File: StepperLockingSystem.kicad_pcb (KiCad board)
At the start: 4 copper layers, 35.5 x 35.5 mm, 77 parts, among them J1 Conn_01x01_Female, J2 Conn_01x01_Female, J3 Conn_01x04_Male, J4 I2C_External, J6 Conn_TempMotor, SW4 SW_Reset, U1 TC1185, U2 SN65HVD232, U3 TMC2209-LA, U5 STM32F103RETx, U6 AS5600, U7 INA180A1, Y1 ABM3B-16MHz

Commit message: [WIP] Create PCB
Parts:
- removed C40, C41: 100nF 35V, Capacitor_SMD:C_0603_1608Metric
- removed J4: I2C_External, Connector_Molex:Molex_PicoBlade_53047-0410_1x04_P1.25mm_Vertical
- removed J6: Conn_TempMotor, Connector_Molex:Molex_PicoBlade_53047-0210_1x02_P1.25mm_Vertical
- removed J_CAN1, J_CAN2: Molex PicoBlade 4Pin, Connector_Molex:Molex_PicoBlade_53047-0410_1x04_P1.25mm_Vertical
- removed OPT1: SX3340, stepperservo:Omron_SX_3340
- removed R23: 10k, Resistor_SMD:R_0603_1608Metric
- removed SW4: SW_Reset, standardContent:SW_SPST_PTS636_SM25F
- added C29: 470pF 100V, Capacitor_SMD:C_0603_1608Metric, F.Cu at (164.0, 86.5)
- added C31: 470pF 100V, Capacitor_SMD:C_0603_1608Metric, F.Cu at (171.4, 79.0)
- added C32: 470pF 100V, Capacitor_SMD:C_0603_1608Metric, F.Cu at (154.4, 94.4)
- added C36: 22nF 50V, Capacitor_SMD:C_0603_1608Metric, F.Cu at (158.4, 96.3)
- added C37: 2.2uF 16V, Capacitor_SMD:C_0603_1608Metric, F.Cu at (168.0, 84.0)
- added C38: 100nF 35V, Capacitor_SMD:C_0603_1608Metric, F.Cu at (168.0, 81.5)
- added J_LED1: Molex PicoBlade, Connector_Molex:Molex_PicoBlade_53047-0410_1x04_P1.25mm_Vertical, F.Cu at (76.4, 19.6)
- added L1: XGL6060-103, Inductor_SMD:L_Coilcraft_XAL60xx_6.36x6.56mm, F.Cu at (196.0, 35.8)
- added Q1: IRF8707, Package_SO:SOIC-8_3.9x4.9mm_P1.27mm, F.Cu at (196.3, 28.5)
- added R17: 1k, Resistor_SMD:R_0603_1608Metric, F.Cu at (160.0, 84.9)
- added R18: 4.7k, Resistor_SMD:R_0603_1608Metric, F.Cu at (160.0, 87.4)
- added R8: 2k, Resistor_SMD:R_0603_1608Metric, F.Cu at (45.8, 57.9)
- added SW1: SW_Reset, extraFootprints:PTS636_F-leads, F.Cu at (42.8, 47.7)
- added U4: AS5600, Package_SO:SOIC-8_3.9x4.9mm_P1.27mm, F.Cu at (41.8, 53.4)
- C10: value 10uF 35V -> 180uF; footprint Capacitor_SMD:C_1206_3216Metric -> Capacitor_THT:CP_Radial_D8.0mm_P2.50mm; moved to F.Cu
- C11: value 10uF 35V -> 22uF; footprint Capacitor_SMD:C_1206_3216Metric -> Capacitor_SMD:C_0805_2012Metric; moved to F.Cu
- C12, C13: value 100nF 35V -> 22uF; footprint Capacitor_SMD:C_0603_1608Metric -> Capacitor_SMD:C_0805_2012Metric; moved to F.Cu
- C14: value 100nF 35V -> 1uF; moved to F.Cu
- C15: value 22nF 50V -> 1u; moved to F.Cu
- C16: value 2.2uF 16V -> 100n; moved to F.Cu
- C17: value 470pF 100V -> 15pF; moved to F.Cu
- C18: value 100nF 35V -> 15pF; moved to F.Cu
- C19: value 470pF 100V -> 100nF; moved to F.Cu
- C2, C28: value 1uF 35V -> 100nF 35V
- C20: value 470pF 100V -> 1uF; moved to F.Cu
- C21: value 100nF 35V -> 100nF; moved to F.Cu
- C22: value 470pF 100V -> 10uF; footprint Capacitor_SMD:C_0603_1608Metric -> Capacitor_SMD:C_1206_3216Metric; moved to F.Cu
- C23: value 100nF 35V -> 100nF
- C24: value 100nF 35V -> 1uF 35V
- C25, C27: value 100nF 35V -> 10uF 35V; footprint Capacitor_SMD:C_0603_1608Metric -> Capacitor_SMD:C_1206_3216Metric
- C3: value 470pF 100V -> 100nF 35V
- C30: value 10nF -> 470pF 100V
- C33: value 15pF -> 330uF 35V; footprint Capacitor_SMD:C_0603_1608Metric -> Capacitor_SMD:CP_Elec_10x10.5
- C34: value 15pF -> 100nF 35V
- C5: value 10uF 35V -> 470pF 100V; footprint Capacitor_SMD:C_1206_3216Metric -> Capacitor_SMD:C_0603_1608Metric
- C6: value 330uF 35V -> 1uF 35V; footprint Capacitor_SMD:CP_Elec_10x10.5 -> Capacitor_SMD:C_0603_1608Metric
- C7: value 100nF 35V -> 1uF
- C8: value 100nF 35V -> 22u 16V; footprint Capacitor_SMD:C_0603_1608Metric -> Capacitor_SMD:C_0805_2012Metric; moved to F.Cu
- C9: value 1uF 35V -> 22u 16V; footprint Capacitor_SMD:C_0603_1608Metric -> Capacitor_SMD:C_0805_2012Metric
- D1: footprint standardContent:LED_LiteOn_LTST-C195TGKRKT -> extraFootprints:LED_LiteOn_LTST-C195TGKRKT
- J1: value Conn_01x01_Female -> Conn_12V; footprint TestPoint:TestPoint_Loop_D2.54mm_Drill1.5mm_Beaded -> Connector_AMASS:AMASS_XT30U-M_1x02_P5.0mm_Vertical
- J2: value Conn_01x01_Female -> Conn_TempMotor; footprint TestPoint:TestPoint_Loop_D2.54mm_Drill1.5mm_Beaded -> Connector_Molex:Molex_PicoBlade_53047-0210_1x02_P1.25mm_Vertical
- R1: value 0.11 -> 10k; footprint Resistor_SMD:R_0612_1632Metric -> Resistor_SMD:R_0603_1608Metric
- R10: value 270m -> 380R; footprint Resistor_SMD:R_0612_1632Metric -> Resistor_SMD:R_0603_1608Metric; moved to F.Cu
- R11: value 10k -> 220R; moved to F.Cu
- R12: value 4k7 -> 10k
- R13: value 4k7 -> 100R
- R14: value 2k -> 100k
- R15: value 2k -> 1.1R 0.5W; footprint Resistor_SMD:R_0603_1608Metric -> Resistor_SMD:R_0805_2012Metric
- R16: value 220 -> 22k; moved to F.Cu
- R19: value 100 -> 13k
- R2: value 120 -> 51m; footprint Resistor_SMD:R_0603_1608Metric -> Resistor_SMD:R_0612_1632Metric
- R20: value 10k -> 180m; footprint Resistor_SMD:R_0603_1608Metric -> Resistor_SMD:R_0612_1632Metric; moved to F.Cu
- R21: value 380 -> 180m; footprint Resistor_SMD:R_0603_1608Metric -> Resistor_SMD:R_0612_1632Metric
- R22: value 220 -> 22k
- R3: value 1.1R 0.5W -> 2k2; footprint Resistor_SMD:R_0805_2012Metric -> Resistor_SMD:R_0603_1608Metric
- R4: value 1k -> 2k2
- R5: value 22k -> 39k; moved to F.Cu
- R6: value 4.7k -> 7k5
- R7: value 22k -> 10k; moved to F.Cu
- R9: value 270m -> 2k; footprint Resistor_SMD:R_0612_1632Metric -> Resistor_SMD:R_0603_1608Metric; moved to F.Cu
- U1: value TC1185 -> INA180A1
- U2: value SN65HVD232 -> TC1185; footprint Package_SO:SOIC-8_3.9x4.9mm_P1.27mm -> Package_TO_SOT_SMD:SOT-23-5; moved to F.Cu
- U3: value TMC2209-LA -> RT8298ZSP; footprint Package_DFN_QFN:QFN-28-1EP_5x5mm_P0.5mm_EP3.35x3.35mm_ThermalVias -> Package_SO:HSOP-8-1EP_3.9x4.9mm_P1.27mm_EP2.41x3.1mm_ThermalVias; moved to F.Cu
- U5: value STM32F103RETx -> 24LC64; footprint Package_QFP:LQFP-64_10x10mm_P0.5mm -> Package_TO_SOT_SMD:SOT-23-5; moved to F.Cu
- U6: value AS5600 -> STM32G0B1KET; footprint Package_SO:SOIC-8_3.9x4.9mm_P1.27mm -> Package_QFP:LQFP-32_7x7mm_P0.8mm; moved to F.Cu
- U7: value INA180A1 -> TMC2209-LA; footprint Package_TO_SOT_SMD:SOT-23-5 -> Package_DFN_QFN:QFN-28-1EP_5x5mm_P0.5mm_EP3.35x3.35mm_ThermalVias
- moved J_SWD1 145.8 mm to (28.7, 59.6), turned to 0 degrees
- moved U5 135.8 mm to (34.4, 64.0), turned to 0 degrees
- moved U6 132.9 mm to (31.9, 50.9), turned to 0 degrees
- moved H4 126.1 mm to (98.0, 13.3)
- moved J1 125.7 mm to (77.5, 12.9)
- moved D1 125.1 mm to (49.4, 59.9), turned to 0 degrees
- moved J2 123.2 mm to (40.0, 59.7)
- moved R14 120.2 mm to (48.0, 51.7), turned to 0 degrees
- moved C23 119.5 mm to (61.4, 46.4), turned to 0 degrees
- moved U1 118.9 mm to (84.4, 27.4), turned to 0 degrees
- moved Y1 116.2 mm to (51.7, 47.8), turned to 0 degrees
- moved C3 115.9 mm to (93.0, 25.5), turned to 0 degrees
- moved C2 115.1 mm to (89.0, 26.4), turned to 0 degrees
- moved R2 114.6 mm to (104.0, 11.8), turned to 0 degrees
- moved U2 113.4 mm to (93.2, 19.5), turned to 0 degrees
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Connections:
- C10 pad 1: VCC -> +5V
- C11 pad 1: VCC -> +5V
- C12 pad 1: VCC -> +5V
- C12 pad 2: /StepperDriver/chargePumpVoltage -> GND
- C13 pad 1: VCC -> +5V
- C14 pad 1: VCC -> Net-(C14-Pad1)
- C15 pad 1: /StepperDriver/chargePumpIn -> +3V3
- C15 pad 2: /StepperDriver/chargePumpOut -> GND
- C16 pad 1: /StepperDriver/internal5VReg -> +3V3
- C17 pad 1: /StepperDriver/coilA_2 -> GND
- C17 pad 2: GND -> Net-(C17-Pad2)
- C18 pad 1: /StepperDriver/senseCoilA -> GND
- C18 pad 2: GND -> Net-(C18-Pad2)
- C19 pad 1: /StepperDriver/coilA_1 -> /MCU/~{RST}
- C2 pad 1: +5V -> /inputCurrent
- C20 pad 1: /StepperDriver/coilB_1 -> +3V3
- C21 pad 1: /StepperDriver/senseCoilB -> +3V3
- C22 pad 1: /StepperDriver/coilB_2 -> GND
- C22 pad 2: GND -> +3V3
- C24 pad 1: GND -> VCC
- C24 pad 2: +3V3 -> Net-(C24-Pad2)
- C25 pad 1: GND -> VCC
- C25 pad 2: +3V3 -> GND
- C26 pad 1: GND -> VCC
- C26 pad 2: +3V3 -> GND
- C27 pad 1: GND -> VCC
- C27 pad 2: +3V3 -> GND
- C28 pad 1: +3V3 -> VCC
- C3 pad 1: Net-(C3-Pad1) -> /inputCurrent
- C30 pad 1: +3V3 -> /StepperDriver/coilA_1
- C33 pad 1: GND -> VCC
- C33 pad 2: Net-(C33-Pad2) -> GND
- C34 pad 1: GND -> +3V3
- C34 pad 2: Net-(C34-Pad2) -> GND
- C35 pad 1: /MCU/~{RST} -> VCC
- C35 pad 2: GND -> /StepperDriver/chargePumpVoltage
- C39 pad 1: +3V3 -> /StepperDriver/senseCoilB
- C4 pad 1: +3V3 -> +5V
- C5 pad 1: GND -> Net-(C5-Pad1)
- C5 pad 2: +3V3 -> GND
- C6 pad 1: VCC -> +3V3
- C7 pad 1: /inputCurrent -> Net-(C7-Pad1)
- C7 pad 2: GND -> Net-(C7-Pad2)
- C8 pad 1: +3V3 -> VCC
- C9 pad 2: Net-(C9-Pad2) -> GND
- J2 pad 1: GND -> +3V3
- J_SWD1 pad 5: /MCU/SWO -> unconnected-(J_SWD1-Pad5)
- R1 pad 1: VCC -> /inputCurrent
- R1 pad 2: Net-(J1-Pad1) -> Net-(R1-Pad2)
- R10 pad 1: GND -> /MCU/LED_RED
- R10 pad 2: /StepperDriver/senseCoilB -> Net-(D1-Pad2)
- R11 pad 1: /StepperDriver/Vref -> /MCU/LED_GREEN
- R11 pad 2: GND -> Net-(D1-Pad1)
- R12 pad 1: /MCU/I2C2_SCL -> /MCU/tempMotor
- R12 pad 2: +3V3 -> GND
- R13 pad 1: +3V3 -> Net-(R13-Pad1)
- R13 pad 2: /MCU/I2C2_SDA -> Net-(C17-Pad2)
- R14 pad 1: +3V3 -> /MCU/SWCLK
- R14 pad 2: /MCU/I2C1_SDA -> GND
- R15 pad 1: +3V3 -> Net-(C24-Pad2)
- R15 pad 2: /MCU/I2C1_SCL -> GND
- R16 pad 1: +5V -> +3V3
- R16 pad 2: Net-(OPT1-Pad1) -> /MCU/~{Stepper_Enable}
- R19 pad 1: Net-(R19-Pad1) -> +3V3
- R19 pad 2: Net-(C33-Pad2) -> /StepperDriver/Vref
- R2 pad 1: Net-(J_CAN1-Pad2) -> VCC
- R2 pad 2: Net-(J_CAN1-Pad1) -> Net-(J1-Pad1)
- R20 pad 1: /MCU/tempMotor -> GND
- R20 pad 2: GND -> /StepperDriver/senseCoilA
- R21 pad 1: /MCU/LED_RED -> GND
- R21 pad 2: Net-(D1-Pad2) -> /StepperDriver/senseCoilB
- R22 pad 1: /MCU/LED_GREEN -> /StepperDriver/Vref
- R22 pad 2: Net-(D1-Pad1) -> GND
- R3 pad 1: Net-(C9-Pad2) -> +5V
- R3 pad 2: GND -> /ledData
- R4 pad 1: Net-(R4-Pad1) -> +5V
- R4 pad 2: /MCU/Stepper_UART -> /ledClock
- R5 pad 1: +3V3 -> +5V
- R5 pad 2: /StepperDriver/~{EN} -> VCC
- R6 pad 1: Net-(R4-Pad1) -> VCC
- R6 pad 2: +3V3 -> GND
- R7 pad 1: +3V3 -> /enableBuck
- R7 pad 2: /StepperDriver/Vref -> GND
- R9 pad 1: GND -> +3V3
- R9 pad 2: /StepperDriver/senseCoilA -> /MCU/I2C1_SDA
- U1 pad 1: +5V -> Net-(R1-Pad2)
- U1 pad 3: +5V -> Net-(J1-Pad1)
- U1 pad 4: Net-(C3-Pad1) -> VCC
- U2 pad 1: /CAN_TX -> +5V
- U2 pad 3: +3V3 -> +5V
- U2 pad 4: /CAN_RX -> Net-(C5-Pad1)
- U2 pad 5: (no net) -> +3V3
- U3 pad 1: /StepperDriver/coilB_2 -> Net-(C7-Pad2)
- U3 pad 2: /StepperDriver/~{EN} -> Net-(C7-Pad1)
- U3 pad 3: GND -> Net-(C14-Pad1)
- U3 pad 4: /StepperDriver/chargePumpOut -> Net-(Q1-Pad4)
- U3 pad 5: /StepperDriver/chargePumpIn -> GND
- U3 pad 6: /StepperDriver/chargePumpVoltage -> VCC
- U3 pad 7: GND -> /enableBuck
- U3 pad 8: /StepperDriver/internal5VReg -> VCC
- U5 pad 1: +3V3 -> /MCU/I2C1_SCL
- U5 pad 2: /MCU/endstopRight -> GND
- U5 pad 3: /StepperDriver/Diag -> /MCU/I2C1_SDA
- U5 pad 4: /StepperDriver/~{EN} -> +3V3
- U5 pad 5: Net-(R19-Pad1) -> GND
- U6 pad 1: +3V3 -> /MCU/LED_GREEN
- U6 pad 2: +3V3 -> Net-(R13-Pad1)
- U6 pad 3: (no net) -> Net-(C18-Pad2)
- U6 pad 4: GND -> +3V3
- U6 pad 6: /MCU/I2C1_SDA -> /MCU/~{RST}
- U6 pad 7: /MCU/I2C1_SCL -> /inputCurrent
- U6 pad 8: GND -> /MCU/tempMotor
- U7 pad 1: Net-(R23-Pad2) -> /StepperDriver/coilB_2
- U7 pad 2: GND -> /MCU/~{Stepper_Enable}
- U7 pad 3: Net-(J1-Pad1) -> GND
- U7 pad 4: VCC -> /StepperDriver/chargePumpOut
- U7 pad 5: +3V3 -> /StepperDriver/chargePumpIn
- Y1 pad 1: Net-(C34-Pad2) -> Net-(C18-Pad2)
- Y1 pad 3: Net-(C33-Pad2) -> Net-(C17-Pad2)
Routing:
- net GND: track 143.2 -> 0.00 mm, vias 40 -> 0
- net +3V3: track 138.7 -> 0.00 mm, vias 12 -> 0
- net +5V: track 85.7 -> 0.00 mm, vias 2 -> 0
- net /MCU/tempMotor: track 53.2 -> 0.00 mm, vias 5 -> 0
- net /MCU/~{RST}: track 47.2 -> 0.00 mm, vias 4 -> 0
- net /MCU/I2C2_SDA: track 33.2 -> 0.00 mm, vias 1 -> 0
- net Net-(R23-Pad2): track 29.2 -> 0.00 mm, vias 2 -> 0
- net /MCU/I2C2_SCL: track 26.7 -> 0.00 mm, vias 1 -> 0
- net /StepperDriver/~{EN}: track 26.5 -> 0.00 mm, vias 3 -> 0
- net /inputCurrent: track 23.8 -> 0.00 mm, vias 3 -> 0
- net /StepperDriver/Direction: track 22.0 -> 0.00 mm
- net /StepperDriver/Diag: track 15.1 -> 0.00 mm
- net Net-(J_CAN1-Pad2): track 14.8 -> 0.00 mm, vias 1 -> 0
- net /StepperDriver/Step: track 14.7 -> 0.00 mm
- net Net-(J_CAN1-Pad1): track 14.0 -> 0.00 mm, vias 1 -> 0
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- removed copper zone on B.Cu, net +3V3
- removed copper zone on B.Cu, net /StepperDriver/coilA_1
- removed copper zone on In1.Cu, net /StepperDriver/coilA_1
- removed copper zone on B.Cu, net /StepperDriver/coilA_2
- removed copper zone on In1.Cu, net /StepperDriver/coilA_2
- removed copper zone on B.Cu, net /StepperDriver/coilB_1
- removed copper zone on In1.Cu, net /StepperDriver/coilB_1
- removed copper zone on B.Cu, net /StepperDriver/coilB_2
- removed copper zone on In1.Cu, net /StepperDriver/coilB_2
- removed copper zone on B.Cu, net /StepperDriver/senseCoilA
- removed copper zone on B.Cu, net /StepperDriver/senseCoilB
- removed copper zone on B.Cu, net GND
- removed copper zone on F.Cu, net GND
- removed copper zone on In1.Cu, net GND
- removed copper zone on In2.Cu, net GND
- removed copper zone on F.Cu, net Net-(J1-Pad1)
- removed copper zone on B.Cu, net VCC
- removed copper zone on F.Cu, net VCC
- removed copper zone on In1.Cu, net VCC
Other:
- board outline removed
- board text removed: "2021"
- board text removed: "A1"
- board text removed: "A2"
- board text removed: "Albrecht"
- board text removed: "B1"
- board text removed: "B2"
- board text removed: "CAN"
- board text removed: "ExtSen"
- board text removed: "Gnd"
- board text removed: "SWD"
- board text removed: "Stepper Servo v1"
- board text removed: "Tmp"
- board text removed: "Vcc"

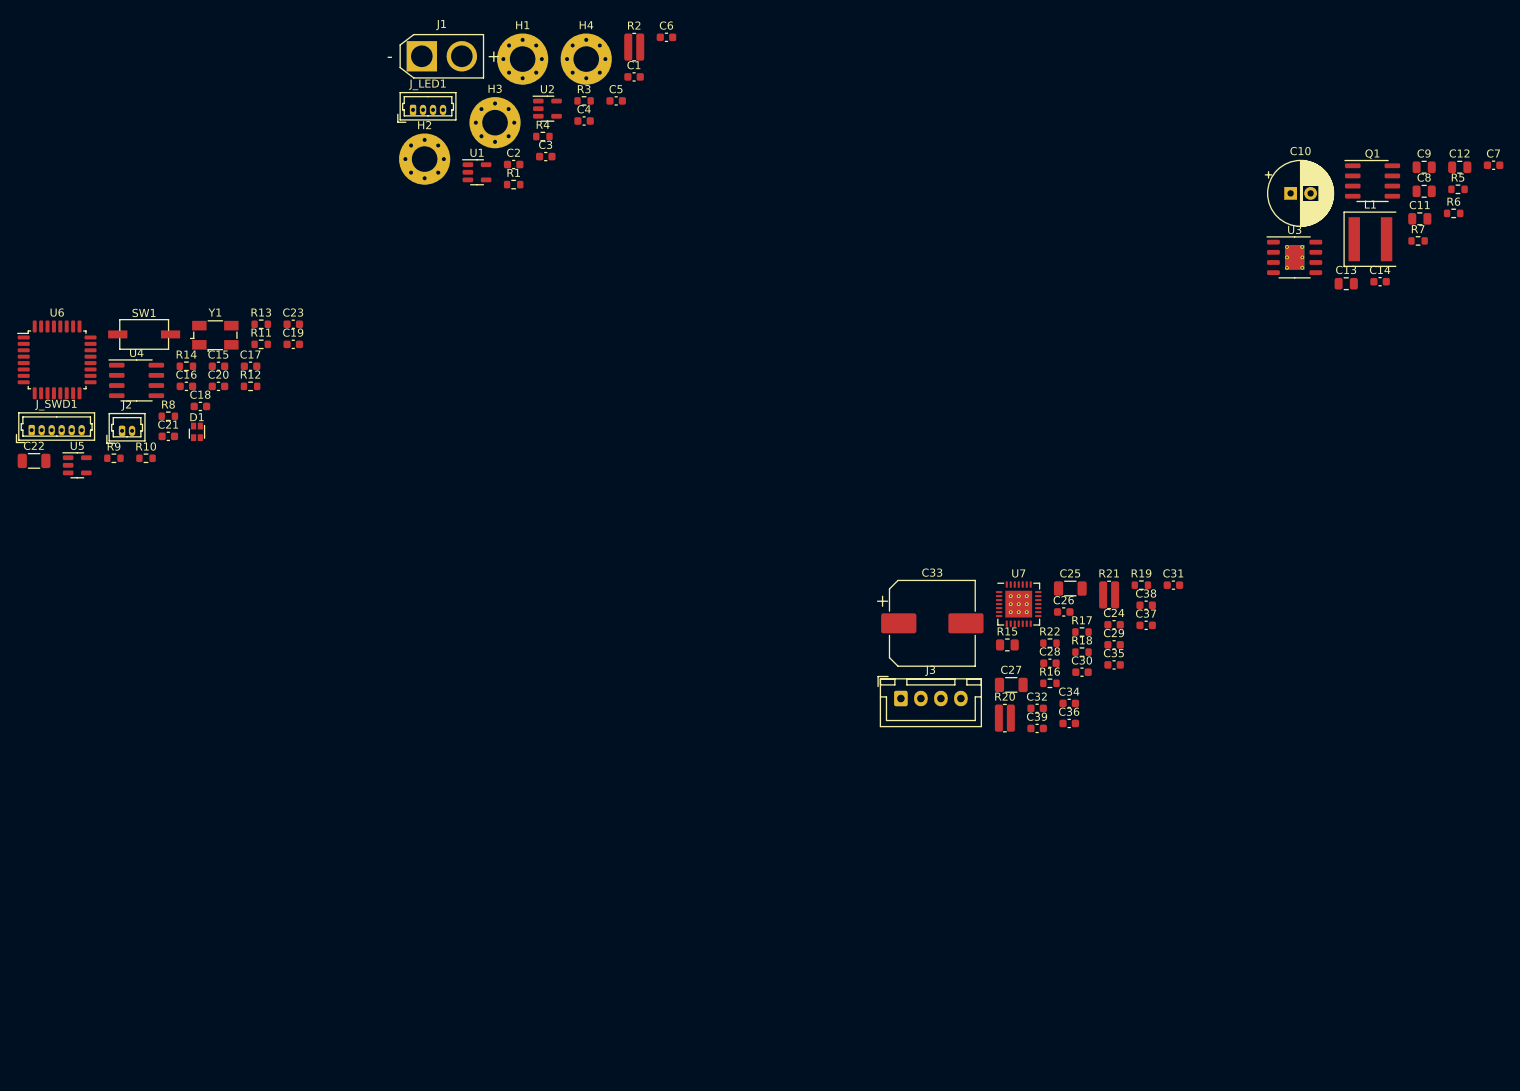
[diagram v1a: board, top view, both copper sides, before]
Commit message: Finish schematic
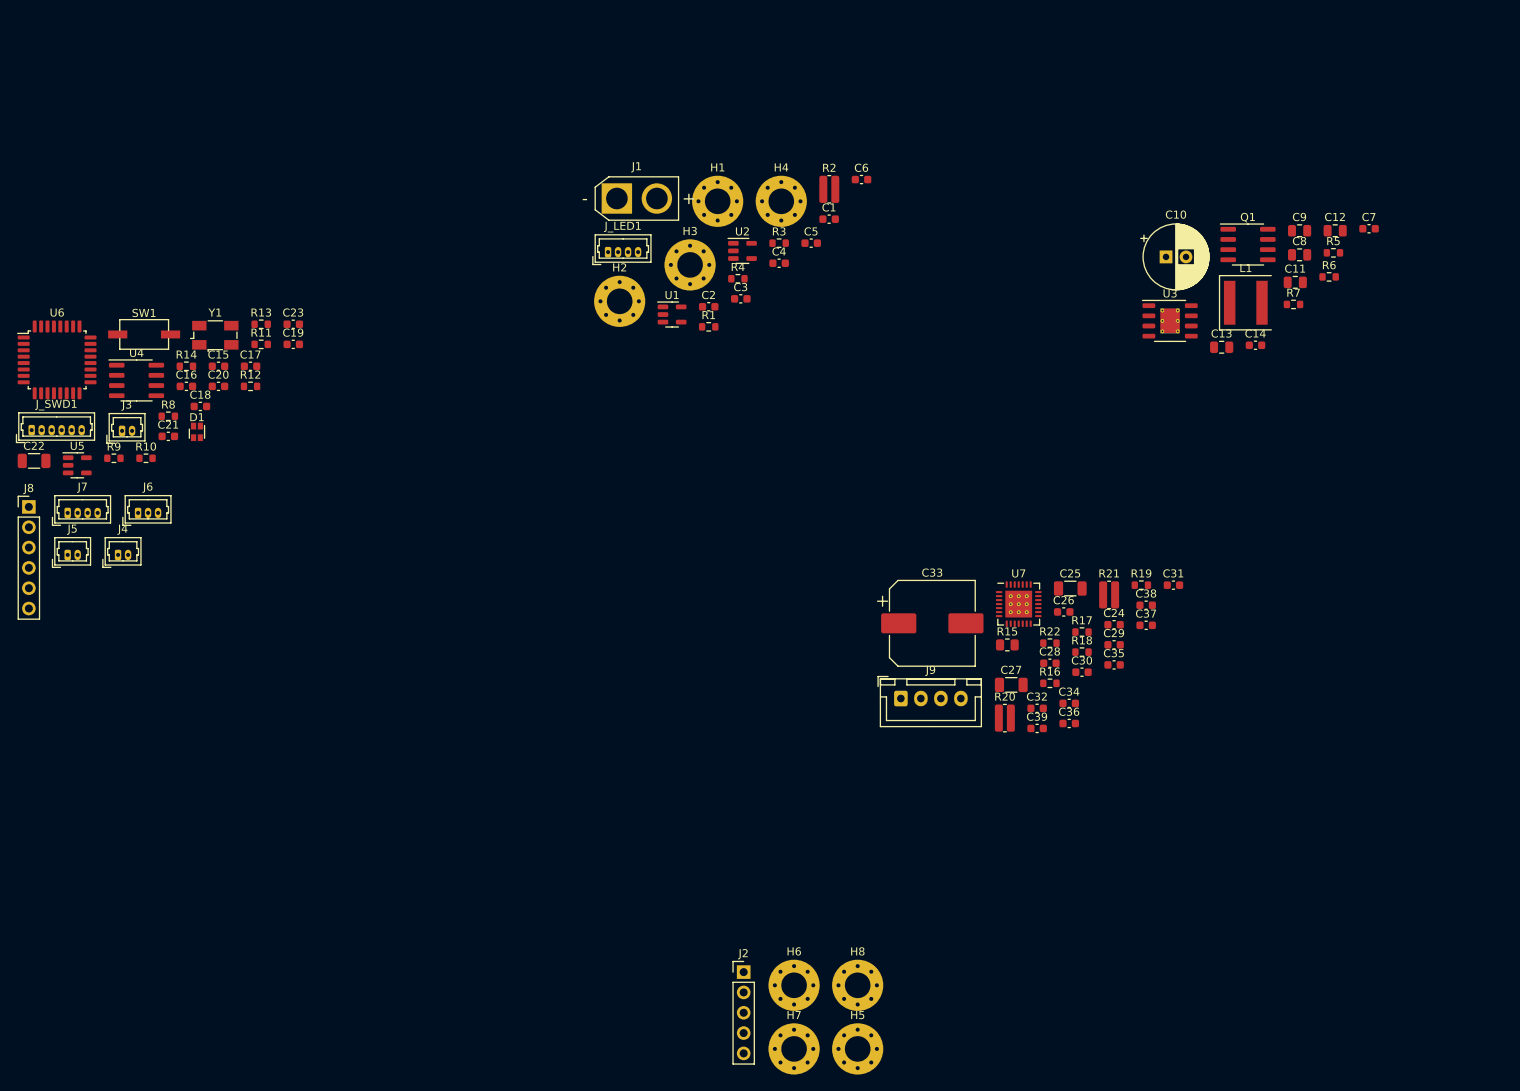
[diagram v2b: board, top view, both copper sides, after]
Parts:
- added H5: MountingHole_Pad, MountingHole:MountingHole_3.2mm_M3_Pad_Via, F.Cu at (131.9, 137.0)
- added H6: MountingHole_Pad, MountingHole:MountingHole_3.2mm_M3_Pad_Via, F.Cu at (124.0, 129.1)
- added H7: MountingHole_Pad, MountingHole:MountingHole_3.2mm_M3_Pad_Via, F.Cu at (124.0, 137.0)
- added H8: MountingHole_Pad, MountingHole:MountingHole_3.2mm_M3_Pad_Via, F.Cu at (131.9, 129.1)
- added J2: 5Pin DuPont 2.54mm, Connector_PinHeader_2.54mm:PinHeader_1x05_P2.54mm_Vertical, F.Cu at (117.7, 127.4)
- added J4: Molex PicoBlade 2Pin, Connector_Molex:Molex_PicoBlade_53047-0210_1x02_P1.25mm_Vertical, F.Cu at (39.5, 75.2)
- added J5: Molex PicoBlade 2Pin, Connector_Molex:Molex_PicoBlade_53047-0210_1x02_P1.25mm_Vertical, F.Cu at (33.2, 75.2)
- added J6: Molex PicoBlade 3Pin, Connector_Molex:Molex_PicoBlade_53047-0310_1x03_P1.25mm_Vertical, F.Cu at (42.0, 70.0)
- added J7: Molex PicoBlade 4Pin, Connector_Molex:Molex_PicoBlade_53047-0410_1x04_P1.25mm_Vertical, F.Cu at (33.2, 70.0)
- added J8: 6Pin DuPont 2.56mm, Connector_PinHeader_2.54mm:PinHeader_1x06_P2.54mm_Vertical, F.Cu at (28.4, 69.2)
- J3: renamed from J2; value Conn_TempMotor -> Molex PicoBlade 2Pin
- moved C3 30.2 mm to (117.3, 43.2)
- moved H1 30.2 mm to (114.5, 31.1)
- moved H4 30.2 mm to (122.4, 31.1)
- moved R2 30.2 mm to (128.4, 29.6)
- moved C6 30.2 mm to (132.4, 28.3)
- moved H2 30.2 mm to (102.2, 43.5)
- moved R4 30.2 mm to (117.0, 40.7)
- moved C1 30.2 mm to (128.4, 33.3)
- moved C2 30.2 mm to (113.3, 44.2)
- moved C4 30.2 mm to (122.1, 38.8)
- moved C5 30.2 mm to (126.1, 36.3)
- moved H3 30.2 mm to (111.0, 39.0)
- moved J1 30.2 mm to (101.8, 30.7)
- moved J_LED1 30.2 mm to (100.8, 37.4)
- moved R1 30.2 mm to (113.3, 46.7)
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- renumbered J3 to J9
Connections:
- U6 pad 10: /MCU/PINA3 -> /MCU/LockState
- U6 pad 12: /MCU/I³C_busy -> /MCU/PINA5
- U6 pad 15: /MCU/PINB0 -> /MCU/CloseButton
- U6 pad 16: /MCU/PINB1 -> /MCU/OpenButton
- U6 pad 17: /MCU/PINB2 -> /MCU/I³C_busy
- U6 pad 9: /MCU/PINA2 -> /MCU/DoorState

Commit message: Add many changes to schematic and WIP PCB
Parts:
- removed C35, C38, C39: 100nF 35V, Capacitor_SMD:C_0603_1608Metric
- removed C36: 22nF 50V, Capacitor_SMD:C_0603_1608Metric
- removed C37: 2.2uF 16V, Capacitor_SMD:C_0603_1608Metric
- removed H8: MountingHole_Pad, MountingHole:MountingHole_3.2mm_M3_Pad_Via
- removed L1: XGL6060-103, Inductor_SMD:L_Coilcraft_XAL60xx_6.36x6.56mm
- added D2: ESD9X5.0ST5G, Diode_SMD:D_SOD-923, F.Cu at (239.8, 99.8)
- added D3: D_Schottky, Diode_SMD:D_SOD-523, F.Cu at (106.3, 54.2)
- added D4: LTST-C195TGKRKT, extraFootprints:LED_LiteOn_LTST-C195TGKRKT, F.Cu at (171.1, 84.2)
- added F1: 2A, extraFootprints:KEYSTONE-FUSE-3557-2, F.Cu at (227.8, 102.9)
- added F2: 2A, extraFootprints:KEYSTONE-FUSE-3557-2, F.Cu at (227.8, 111.0)
- added J10: Conn_01x04_Male, Connector_JST:JST_XH_B4B-XH-A_1x04_P2.50mm_Vertical, F.Cu at (129.7, 125.2)
- added R23: 180m, Resistor_SMD:R_0612_1632Metric, B.Cu at (132.9, 118.7)
- added R24: 22k, Resistor_SMD:R_0603_1608Metric, B.Cu at (139.4, 126.7)
- added TP1: TestPoint, TestPoint:TestPoint_Pad_D2.0mm, F.Cu at (211.1, 138.6)
- added TP10: TestPoint, TestPoint:TestPoint_Pad_D2.0mm, F.Cu at (207.0, 138.6)
- added TP11: TestPoint, TestPoint:TestPoint_Pad_D2.0mm, F.Cu at (223.2, 130.5)
- added TP12: TestPoint, TestPoint:TestPoint_Pad_D2.0mm, F.Cu at (211.1, 130.5)
- added TP13: TestPoint, TestPoint:TestPoint_Pad_D2.0mm, F.Cu at (223.2, 134.6)
- added TP14: TestPoint, TestPoint:TestPoint_Pad_D2.0mm, F.Cu at (219.2, 134.6)
- added TP2: TestPoint, TestPoint:TestPoint_Pad_D2.0mm, F.Cu at (207.0, 130.5)
- added TP3: TestPoint, TestPoint:TestPoint_Pad_D2.0mm, F.Cu at (215.1, 130.5)
- added TP4: TestPoint, TestPoint:TestPoint_Pad_D2.0mm, F.Cu at (211.1, 134.6)
- added TP5: TestPoint, TestPoint:TestPoint_Pad_D2.0mm, F.Cu at (207.0, 134.6)
- added TP6: TestPoint, TestPoint:TestPoint_Pad_D2.0mm, F.Cu at (215.1, 138.6)
- added TP7: TestPoint, TestPoint:TestPoint_Pad_D2.0mm, F.Cu at (219.2, 130.5)
- added TP8: TestPoint, TestPoint:TestPoint_Pad_D2.0mm, F.Cu at (215.1, 134.6)
- added TP9: TestPoint, TestPoint:TestPoint_Pad_D2.0mm, F.Cu at (219.2, 138.6)
- C10: value 180uF -> 15pF; footprint Capacitor_THT:CP_Radial_D8.0mm_P2.50mm -> Capacitor_SMD:C_0603_1608Metric
- C11: value 22uF -> 15pF; footprint Capacitor_SMD:C_0805_2012Metric -> Capacitor_SMD:C_0603_1608Metric
- C12: value 22uF -> 100nF; footprint Capacitor_SMD:C_0805_2012Metric -> Capacitor_SMD:C_0603_1608Metric
- C13: value 22uF -> 1uF; footprint Capacitor_SMD:C_0805_2012Metric -> Capacitor_SMD:C_0603_1608Metric; moved to B.Cu
- C14: value 1uF -> 100nF; moved to B.Cu
- C15: value 1u -> 100nF
- C16: value 100n -> 100nF
- C17: value 15pF -> 10uF; footprint Capacitor_SMD:C_0603_1608Metric -> Capacitor_SMD:C_1206_3216Metric; moved to B.Cu
- C18: value 15pF -> 100nF; moved to B.Cu
- C19: value 100nF -> 1uF 16V; moved to B.Cu
- C20: value 1uF -> 10uF 16V; footprint Capacitor_SMD:C_0603_1608Metric -> Capacitor_SMD:C_1206_3216Metric; moved to B.Cu
- C21, C23: value 100nF -> 100nF 16V; moved to B.Cu
- C22: value 10uF -> 10uF 16V; moved to B.Cu
- C24: value 1uF 35V -> 470pF 100V; moved to B.Cu
- C25, C27: value 10uF 35V -> 470pF 100V; footprint Capacitor_SMD:C_1206_3216Metric -> Capacitor_SMD:C_0603_1608Metric; moved to B.Cu
- C26: value 100nF 35V -> 470pF 100V; moved to B.Cu
- C28: value 100nF 35V -> 330uF 16V; footprint Capacitor_SMD:C_0603_1608Metric -> Capacitor_SMD:CP_Elec_10x10.5
- C29, C30: value 470pF 100V -> 100nF 16V; moved to B.Cu
- C31: value 470pF 100V -> 22nF 50V; moved to B.Cu
- C32: value 470pF 100V -> 2.2uF 16V; moved to B.Cu
- C33: value 330uF 35V -> 100nF 35V; footprint Capacitor_SMD:CP_Elec_10x10.5 -> Capacitor_SMD:C_0603_1608Metric; moved to B.Cu
- C34, U7: moved to B.Cu
- C7: value 1uF -> 100n; moved to B.Cu
- C8: value 22u 16V -> 1uF 16V; footprint Capacitor_SMD:C_0805_2012Metric -> Capacitor_SMD:C_0603_1608Metric
- C9: value 22u 16V -> 1uF; footprint Capacitor_SMD:C_0805_2012Metric -> Capacitor_SMD:C_0603_1608Metric
- D1: value LTST-C195TGKRKT -> ESD9X12ST5G; footprint extraFootprints:LED_LiteOn_LTST-C195TGKRKT -> Diode_SMD:D_SOD-923
- H1, H2, H3, H4, H5, H6, H7: footprint MountingHole:MountingHole_3.2mm_M3_Pad_Via -> MountingHole:MountingHole_3.2mm_M3_ISO14580
- J1: value Conn_12V -> Phoenix Contact MSTB 4 Pin; footprint Connector_AMASS:AMASS_XT30U-M_1x02_P5.0mm_Vertical -> Connector_Phoenix_MSTB:PhoenixContact_MSTBVA_2,5_4-G-5,08_1x04_P5.08mm_Vertical
- J4: value Molex PicoBlade 2Pin -> Molex PicoBlade 4Pin; footprint Connector_Molex:Molex_PicoBlade_53047-0210_1x02_P1.25mm_Vertical -> Connector_Molex:Molex_PicoBlade_53047-0410_1x04_P1.25mm_Vertical
- J6: value Molex PicoBlade 3Pin -> 6Pin DuPont 2.56mm; footprint Connector_Molex:Molex_PicoBlade_53047-0310_1x03_P1.25mm_Vertical -> Connector_PinHeader_2.54mm:PinHeader_1x07_P2.54mm_Vertical
- J7: value Molex PicoBlade 4Pin -> Molex PicoBlade 2Pin; footprint Connector_Molex:Molex_PicoBlade_53047-0410_1x04_P1.25mm_Vertical -> Connector_Molex:Molex_PicoBlade_53047-0210_1x02_P1.25mm_Vertical
- J8: value 6Pin DuPont 2.56mm -> Molex PicoBlade 3Pin; footprint Connector_PinHeader_2.54mm:PinHeader_1x06_P2.54mm_Vertical -> Connector_Molex:Molex_PicoBlade_53047-0310_1x03_P1.25mm_Vertical
- J9: value Conn_01x04_Male -> Molex PicoBlade 2Pin; footprint Connector_JST:JST_XH_B4B-XH-A_1x04_P2.50mm_Vertical -> Connector_Molex:Molex_PicoBlade_53047-0210_1x02_P1.25mm_Vertical
- Q1: value IRF8707 -> IRLML0030; footprint Package_SO:SOIC-8_3.9x4.9mm_P1.27mm -> Package_TO_SOT_SMD:SOT-23
- R10: value 380R -> 220R
- R11: value 220R -> 10k; moved to B.Cu
- R12: value 10k -> 100k
- R13: value 100R -> 5k
- R14: value 100k -> 5k
- R15: value 1.1R 0.5W -> 5k; footprint Resistor_SMD:R_0805_2012Metric -> Resistor_SMD:R_0603_1608Metric
- R16: value 22k -> 5k
- R17: value 1k -> 1.1R 0.5W; footprint Resistor_SMD:R_0603_1608Metric -> Resistor_SMD:R_0805_2012Metric; moved to B.Cu
- R18: value 4.7k -> 22k; moved to B.Cu
- R19: value 13k -> 1k; moved to B.Cu
- R2: value 51m -> 100m 0.5W
- R20: value 180m -> 4.7k; footprint Resistor_SMD:R_0612_1632Metric -> Resistor_SMD:R_0603_1608Metric; moved to B.Cu
- R21: value 180m -> 13k; footprint Resistor_SMD:R_0612_1632Metric -> Resistor_SMD:R_0603_1608Metric; moved to B.Cu
- R22: value 22k -> 180m; footprint Resistor_SMD:R_0603_1608Metric -> Resistor_SMD:R_0612_1632Metric; moved to B.Cu
- R5: value 39k -> 2k; moved to B.Cu
- R6: value 7k5 -> 2k; moved to B.Cu
- R7: value 10k -> 1k
- R8: value 2k -> 100R
- R9: value 2k -> 380R
- U3: value RT8298ZSP -> 24LC64; footprint Package_SO:HSOP-8-1EP_3.9x4.9mm_P1.27mm_EP2.41x3.1mm_ThermalVias -> Package_TO_SOT_SMD:SOT-23-5; moved to B.Cu
- U4: value AS5600 -> STM32G0B1KET; footprint Package_SO:SOIC-8_3.9x4.9mm_P1.27mm -> Package_QFP:LQFP-32_7x7mm_P0.8mm
- U5: value 24LC64 -> USBLC6-2SC6; footprint Package_TO_SOT_SMD:SOT-23-5 -> Package_TO_SOT_SMD:SOT-23-6
- U6: value STM32G0B1KET -> USBLC6-2SC6; footprint Package_QFP:LQFP-32_7x7mm_P0.8mm -> Package_TO_SOT_SMD:SOT-23-6
- moved H7 232.5 mm to (355.2, 112.5)
- moved J2 205.6 mm to (323.2, 129.6), turned to 180 degrees
- moved C18 201.3 mm to (248.5, 89.0), turned to 180 degrees
- moved R11 201.0 mm to (255.8, 81.2), turned to 180 degrees
- moved U6 200.6 mm to (219.9, 120.9)
- moved H6 199.9 mm to (323.2, 112.5)
- moved U5 198.9 mm to (225.0, 120.9)
- moved C17 196.5 mm to (248.5, 91.2), turned to 180 degrees
- moved R14 195.5 mm to (227.2, 129.7)
- moved D1 194.9 mm to (239.8, 101.8)
- moved C15 192.8 mm to (227.2, 132.2)
- moved H5 191.3 mm to (323.2, 136.5)
- moved R13 187.7 mm to (219.0, 141.9)
- moved C16 181.6 mm to (207.0, 141.9)
- moved J_SWD1 155.4 mm to (180.6, 92.5), turned to 180 degrees
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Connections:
- C10 pad 1: +5V -> GND
- C10 pad 2: GND -> Net-(C10-Pad2)
- C11 pad 1: +5V -> GND
- C11 pad 2: GND -> Net-(C11-Pad2)
- C12 pad 1: +5V -> /MCU/~{RST}
- C13 pad 1: +5V -> +3V3
- C14 pad 1: Net-(C14-Pad1) -> +3V3
- C15 pad 1: +3V3 -> GND
- C15 pad 2: GND -> +5V
- C16 pad 1: +3V3 -> GND
- C16 pad 2: GND -> +5V
- C17 pad 2: Net-(C17-Pad2) -> +3V3
- C18 pad 2: Net-(C18-Pad2) -> +3V3
- C19 pad 1: /MCU/~{RST} -> VCC
- C19 pad 2: GND -> Net-(C19-Pad2)
- C20 pad 1: +3V3 -> VCC
- C21 pad 1: +3V3 -> VCC
- C22 pad 1: GND -> VCC
- C22 pad 2: +3V3 -> GND
- C23 pad 1: GND -> VCC
- C23 pad 2: +3V3 -> GND
- C24 pad 1: VCC -> /StepperDriver/coilA_2
- C24 pad 2: Net-(C24-Pad2) -> GND
- C25 pad 1: VCC -> /StepperDriver/coilA_1
- C26 pad 1: VCC -> /StepperDriver/coilB_1
- C27 pad 1: VCC -> /StepperDriver/coilB_2
- C29 pad 1: /StepperDriver/coilA_2 -> +3V3
- C30 pad 1: /StepperDriver/coilA_1 -> VCC
- C30 pad 2: GND -> /StepperDriver/chargePumpVoltage
- C31 pad 1: /StepperDriver/coilB_1 -> /StepperDriver/chargePumpIn
- C31 pad 2: GND -> /StepperDriver/chargePumpOut
- C32 pad 1: /StepperDriver/coilB_2 -> /StepperDriver/internal5VReg
- C33 pad 1: VCC -> /StepperDriver/senseCoilA
- C34 pad 1: +3V3 -> /StepperDriver/senseCoilB
- C7 pad 1: Net-(C7-Pad1) -> +3V3
- C7 pad 2: Net-(C7-Pad2) -> GND
- C9 pad 1: VCC -> Net-(C9-Pad1)
- D1 pad 2: Net-(D1-Pad2) -> GND
- J1 pad 1: Net-(J1-Pad1) -> Net-(F1-Pad1)
- J3 pad 1: +3V3 -> VCC
- J3 pad 2: /MCU/tempMotor -> Net-(D3-Pad2)
- J4 pad 1: /MCU/DoorState -> +3V3
- J4 pad 2: GND -> /MCU/I²C1_SCL
- J5 pad 1: /MCU/LockState -> +3V3
- J5 pad 2: GND -> /MCU/tempMotor
- J6 pad 1: /MCU/CloseButton -> +3V3
- J6 pad 2: /MCU/OpenButton -> +5V
- J6 pad 3: GND -> /MCU/PINB7
- J7 pad 1: /MCU/I²C2_SDA -> +5V
- J7 pad 2: /MCU/I²C2_SCL -> Net-(J7-Pad2)
- J8 pad 1: +3V3 -> +5V
- J8 pad 2: +5V -> Net-(J8-Pad2)
- J8 pad 3: /MCU/PINA4 -> Net-(J8-Pad3)
- J9 pad 1: /StepperDriver/coilA_2 -> +5V
- J9 pad 2: /StepperDriver/coilA_1 -> Net-(J9-Pad2)
- Q1 pad 2: GND -> Net-(C9-Pad1)
- Q1 pad 3: GND -> Net-(D3-Pad2)
- R10 pad 1: /MCU/LED_RED -> /MCU/LED_GREEN
- R10 pad 2: Net-(D1-Pad2) -> Net-(D4-Pad1)
- R11 pad 1: /MCU/LED_GREEN -> /MCU/tempMotor
- R11 pad 2: Net-(D1-Pad1) -> GND
- R12 pad 1: /MCU/tempMotor -> /MCU/SWCLK
- R13 pad 1: Net-(R13-Pad1) -> Net-(J8-Pad2)
- R13 pad 2: Net-(C17-Pad2) -> GND
- R14 pad 1: /MCU/SWCLK -> Net-(J8-Pad3)
- R15 pad 1: Net-(C24-Pad2) -> Net-(J9-Pad2)
- R16 pad 1: +3V3 -> Net-(J7-Pad2)
- R16 pad 2: /MCU/~{Stepper_Enable} -> GND
- R17 pad 1: Net-(R17-Pad1) -> Net-(C19-Pad2)
- R17 pad 2: /MCU/Stepper_UART -> GND
- R18 pad 1: Net-(R17-Pad1) -> +3V3
- R18 pad 2: +3V3 -> /MCU/~{Stepper_Enable}
- R19 pad 1: +3V3 -> Net-(R19-Pad1)
- R19 pad 2: /StepperDriver/Vref -> /MCU/Stepper_UART
- R2 pad 2: Net-(J1-Pad1) -> Net-(D1-Pad1)
- R20 pad 1: GND -> Net-(R19-Pad1)
- R20 pad 2: /StepperDriver/senseCoilA -> +3V3
- R21 pad 1: GND -> +3V3
- R21 pad 2: /StepperDriver/senseCoilB -> /StepperDriver/Vref
- R22 pad 1: /StepperDriver/Vref -> GND
- R22 pad 2: GND -> /StepperDriver/senseCoilA
- R5 pad 1: +5V -> +3V3
- R5 pad 2: VCC -> /MCU/I²C1_SCL
- R6 pad 1: VCC -> +3V3
- R6 pad 2: GND -> /MCU/I²C1_SDA
- R7 pad 1: /enableBuck -> Net-(C9-Pad1)
- R7 pad 2: GND -> /MCU/LockState
- R8 pad 1: +3V3 -> Net-(R8-Pad1)
- R8 pad 2: /MCU/I2C1_SCL -> Net-(C10-Pad2)
- R9 pad 1: +3V3 -> /MCU/LED_RED
- R9 pad 2: /MCU/I2C1_SDA -> Net-(D4-Pad2)
- U1 pad 3: Net-(J1-Pad1) -> Net-(D1-Pad1)
- U3 pad 1: Net-(C7-Pad2) -> /MCU/I²C1_SCL
- U3 pad 2: Net-(C7-Pad1) -> GND
- U3 pad 3: Net-(C14-Pad1) -> /MCU/I²C1_SDA
- U3 pad 4: Net-(Q1-Pad4) -> +3V3
- U4 pad 1: +3V3 -> /MCU/PINB9
- U4 pad 2: +3V3 -> Net-(R8-Pad1)
- U4 pad 3: unconnected-(U4-Pad3) -> Net-(C11-Pad2)
- U4 pad 4: GND -> +3V3
- U4 pad 6: /MCU/I2C1_SDA -> /MCU/~{RST}
- U4 pad 7: /MCU/I2C1_SCL -> /MCU/Stepper_Step
- U4 pad 8: GND -> /MCU/tempMotor
- U5 pad 1: /MCU/I2C1_SCL -> /MCU/LockState
- U5 pad 3: /MCU/I2C1_SDA -> /MCU/DoorState
- U5 pad 4: +3V3 -> Net-(J7-Pad2)
- U5 pad 5: GND -> +5V
- U6 pad 1: /MCU/LED_GREEN -> /MCU/OpenButton
- U6 pad 2: Net-(R13-Pad1) -> GND
- U6 pad 3: Net-(C18-Pad2) -> /MCU/CloseButton
- U6 pad 4: +3V3 -> Net-(J8-Pad2)
- U6 pad 5: GND -> +5V
- U6 pad 6: /MCU/~{RST} -> Net-(J8-Pad3)
- U7 pad 14: Net-(R17-Pad1) -> Net-(R19-Pad1)
- Y1 pad 1: Net-(C18-Pad2) -> Net-(C11-Pad2)
- Y1 pad 3: Net-(C17-Pad2) -> Net-(C10-Pad2)
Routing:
- net /MCU/~{RST}: track 0.00 -> 59.0 mm, vias 0 -> 2
- net VCC: track 0.00 -> 36.1 mm, vias 0 -> 14
- net /MCU/SWDIO: track 0.00 -> 33.3 mm
- net /MCU/SWCLK: track 0.00 -> 31.6 mm
- net /MCU/Stepper_UART: track 0.00 -> 30.6 mm, vias 0 -> 3
- net Net-(D1-Pad1): track 0.00 -> 28.3 mm, vias 0 -> 2
- net /MCU/Stepper_Direction: track 0.00 -> 27.5 mm, vias 0 -> 2
- net /MCU/LED_RED: track 0.00 -> 27.1 mm
- net /MCU/LED_GREEN: track 0.00 -> 27.0 mm
- net +5V: track 0.00 -> 23.7 mm
- net /MCU/~{Stepper_Enable}: track 0.00 -> 22.9 mm, vias 0 -> 1
- net /MCU/Stepper_Diag: track 0.00 -> 21.8 mm, vias 0 -> 2
- net /ledClock: track 0.00 -> 19.9 mm, vias 0 -> 2
- net /ledData: track 0.00 -> 19.6 mm, vias 0 -> 2
- net +3V3: track 0.00 -> 16.1 mm, vias 0 -> 2
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- added copper zone on B.Cu, net /StepperDriver/coilA_1
- added copper zone on B.Cu, net /StepperDriver/coilA_2
- added copper zone on In1.Cu, net /StepperDriver/coilA_2
- added copper zone on B.Cu, net /StepperDriver/coilB_1
- added copper zone on B.Cu, net /StepperDriver/coilB_2
- added copper zone on In1.Cu, net /StepperDriver/coilB_2
- added copper zone on B.Cu, net /StepperDriver/senseCoilA
- added copper zone on B.Cu, net /StepperDriver/senseCoilB
- added copper zone on B.Cu, net GND
- added copper zone on F.Cu, net GND
- added copper zone on F.Cu, net Net-(F1-Pad1)
- added copper zone on B.Cu, net VCC
- added copper zone on F.Cu, net VCC
- added copper zone on In1.Cu, net VCC
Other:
- board outline added: 60 x 60 mm
